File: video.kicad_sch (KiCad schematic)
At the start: 35 parts, among them IC903 HUC6260, Q902 25C945, Q903 25A733, Q904 25C945

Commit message: Add markings for SMD Ds and Qs.
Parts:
- Q902, Q904: value 25C945 -> L6
- Q903: value 25A733 -> M6
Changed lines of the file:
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@@
       (effects (font (size 1.27 1.27)) (justify left))
     )
-    (property "Value" "25C945" (at 250.19 83.82 0)
+    (property "Value" "L6" (at 250.19 83.82 0)
       (effects (font (size 1.27 1.27)) (justify left))
     )
@@
       (effects (font (size 1.27 1.27)) (justify left))
     )
-    (property "Value" "25C945" (at 274.32 93.98 0)
+    (property "Value" "L6" (at 274.32 93.98 0)
       (effects (font (size 1.27 1.27)) (justify left))
     )
@@
       (effects (font (size 1.27 1.27)) (justify left))
     )
-    (property "Value" "25A733" (at 257.81 103.505 0)
-      (effects (font (size 1.27 1.27)) (justify left))
-    )
+    (property "Value" "M6" (at 257.81 103.505 0)
+      (effects (font (size 1.27 1.27)) (justify left))
+    )

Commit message: More schematic clean-up/annotation.
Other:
- company: (none) -> By Cosam
- title: PC Engine Video Encoding -> PC Engine Duo Video Encoding
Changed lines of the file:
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@@
   (paper "A3")
   (title_block
-    (title "PC Engine Video Encoding")
-    (date "2023-11-01")
-    (rev "1.0")
-    (comment 1 "Reverse engineered from original PWA-3285-A board by Cosam")
-    (comment 3 "WORK IN PROGRESS")
+    (title "PC Engine Duo Video Encoding")
+    (date "2023-11-03")
+    (rev "1.1")
+    (company "By Cosam")
+    (comment 1 "https://github.com/Board-Folk/PC-Engine-Duo")
+    (comment 2 "For contributions or corrections please visit:")
+    (comment 3 "Additional parts reverse engineered from original PWA-3285-A board.")
+    (comment 4 "Parts common to PC Engine adapted from TurboGrafx-16 schematics.")
   )
   (junction (at 210.82 144.78) (diameter 0) (color 0 0 0 0)

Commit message: Correct some values/references.
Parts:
- R103: value 20 -> 22
- R104: value 5.2K -> 6.2K
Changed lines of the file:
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@@
       (effects (font (size 1.27 1.27)))
     )
-    (property "Value" "5.2K" (at 222.25 74.93 90)
+    (property "Value" "6.2K" (at 222.25 74.93 90)
       (effects (font (size 1.27 1.27)))
     )
@@
   (symbol (lib_id "Device:R") (at 284.48 85.09 0) (unit 1)
     (in_bom yes) (on_board yes) (dnp no)
-    (property "Reference" "R103" (at 279.4 87.63 90)
+    (property "Reference" "R103" (at 288.29 83.82 0)
       (effects (font (size 1.27 1.27)) (justify left))
     )
-    (property "Value" "20" (at 281.94 87.63 90)
+    (property "Value" "22" (at 288.29 86.36 0)
       (effects (font (size 1.27 1.27)) (justify left))
     )

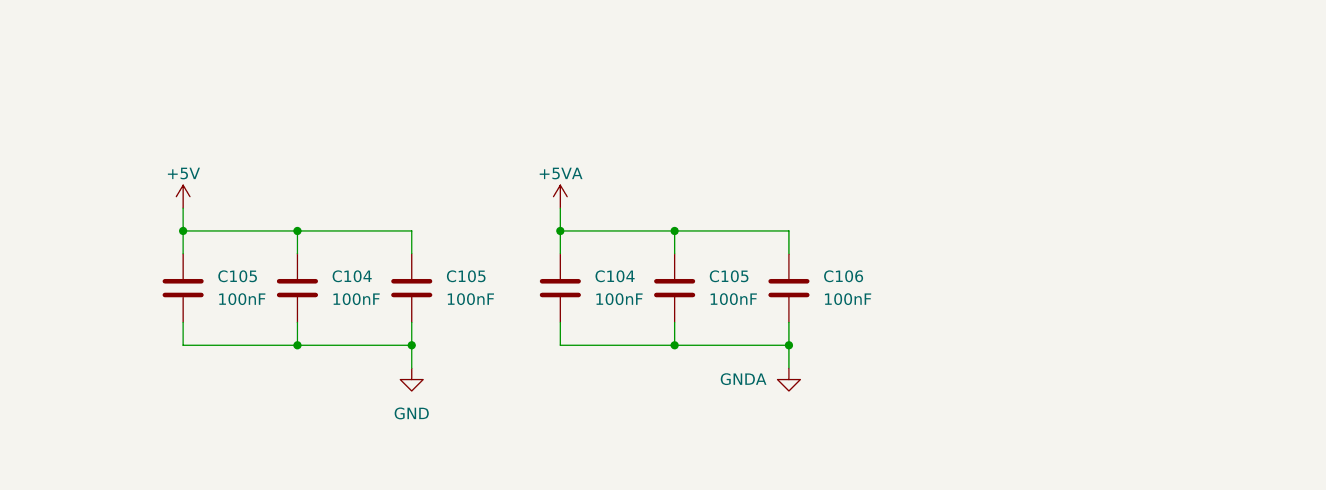
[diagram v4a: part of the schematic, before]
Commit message: Minor schematic/silkscreen changes.
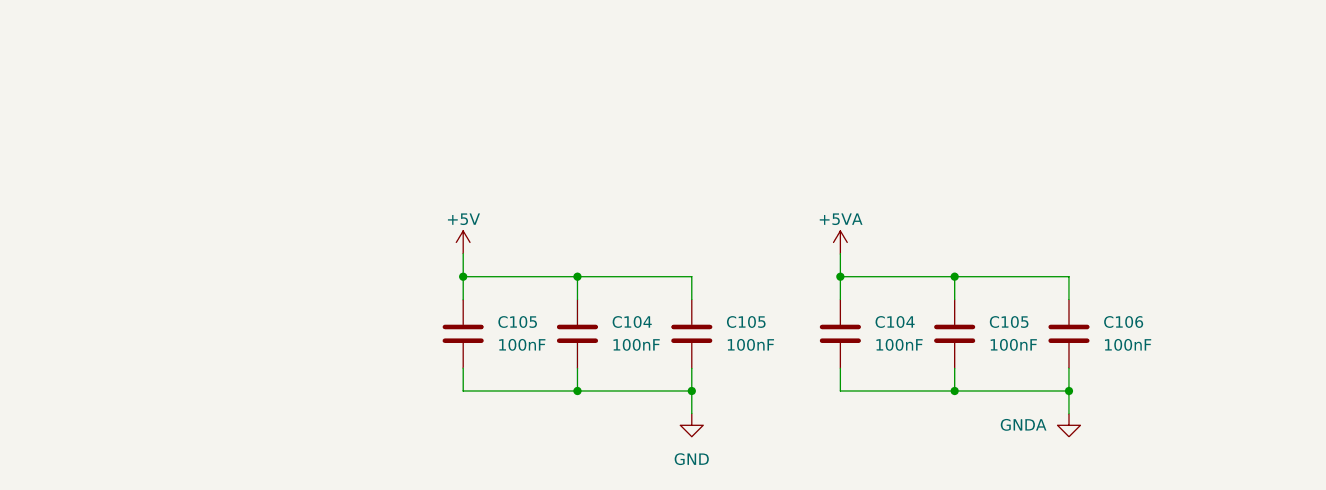
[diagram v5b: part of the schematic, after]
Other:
- moved on the sheet: C104, C105, C106
